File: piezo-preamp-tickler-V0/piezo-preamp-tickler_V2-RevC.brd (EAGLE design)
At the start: 160 x 100 mm, 41 parts, among them IC1 OPA2134UA, Q1 J201SOT-23, Q2 J201SOT-23, SW2-SPST INPUT-select

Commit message: piezo with buffer, mems with dual gain
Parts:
- removed D4: MMSZ5231B, CMU-ArtFab:SOD123
- removed D5: 1N4148, adafruit:SOD-123
- removed U$2: SWITCH_DPDT, CMU-ArtFab:SWITCH_DPDT_CL-SB-22B
- removed U$4: (no value), CMU-ArtFab:TRIMPOT-BOURNS-3306F
- added C5: 10uF, adafruit:C0805K
- added R18: 1M, adafruit:TC33X
- added SW1-DPDT: OUTPUT-select, microbuilder:DPDT_SMT_JS202011SCQN
- C1: value 150uF -> 10uF; device rcl:TT5D7L -> adafruit:C0805K
- C2: value 10uF -> 0.1uF
- C3: device adafruit:C0603 -> adafruit:C0805K
- C4: value 100uF -> 150uF; device rcl:TT5D7L -> adafruit:C050-024X044
- D1, D2: value MMSZ5231B -> (none); device CMU-ArtFab:SOD123 -> diode:SOD123
- D3: value MMSZ5231B -> 1N4148; device CMU-ArtFab:SOD123 -> adafruit:SOD-123
- R1: value 10M -> 2.2K
- R10: value 20K -> 1K; device adafruit:TC33X -> CMU-ArtFab:R0603
- R11: value 1K -> 10K
- R12: value 1M -> 390; device CMU-ArtFab:R0603 -> CMU-ArtFab:R0805
- R13: value 1.2K -> 10M
- R14: value 2.2K -> 1.2K
- R15: value 10 -> 1K
- R16: value 390 -> 10
- R3: value 10K -> 1M
- R9: value 1K -> 20K; device CMU-ArtFab:R0603 -> adafruit:TC33X
- moved D1 169.7 mm to (99.1, -1.27)
- moved D2 164.3 mm to (91.4, -1.27), turned to 0 degrees
- moved R1 153.8 mm to (90.2, 11.4), turned to 0 degrees
- moved R3 145.0 mm to (80.0, 6.35), turned to 0 degrees
- moved C1 141.6 mm to (74.9, -1.27), turned to 270 degrees
- moved R2 140.7 mm to (80.0, 11.4), turned to 0 degrees
- moved Q2 136.7 mm to (87.6, 6.35), turned to 180 degrees
- moved R7 131.4 mm to (74.9, 5.08), turned to 90 degrees
- moved R9 130.7 mm to (72.4, 10.2), turned to 180 degrees
- moved R17 128.8 mm to (80.0, -1.27)
- moved C6 123.3 mm to (54.6, 0.00), turned to 270 degrees
- moved Q1 122.6 mm to (50.8, 0.00)
- moved R10 115.3 mm to (80.0, 2.54)
- moved R11 110.8 mm to (59.7, 10.2)
- moved R12 100.5 mm to (34.3, -1.27), turned to 180 degrees
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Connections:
- net HEADSET-MIC renamed N$12
- removed net AMPILFIED-PIEZO: Q2.1, R14.2, SW2-SPST.P$3
- removed net N$1 (its old number): D3.A, D4.A
- new net SELECT: Q2.1, R1.2, SW2-SPST.P$3
- net +12V: now also D3.A; no longer D5.A
- net GND: now also C2.2, C4.2, C5.2, D2.C, R18.2, R3.1; no longer C1.-, C4.-, D1.C, D3.C, R12.1
- net N$10: now also D1.C, R10.1, R3.2; no longer D4.C, R11.1, R12.2
- net N$11: now also C1.2, R10.2, SW1-DPDT.P$3, SW1-DPDT.P$4; no longer C2.2, R11.2, U$2.3, U$2.6
- net N$13: now also SW1-DPDT.P$5; no longer U$2.5
- net N$14: now also C4.1, R14.2; no longer C1.+, R2.2
- net N$15: now also SW1-DPDT.P$2; no longer U$2.2
- net N$16: now also C5.1, D3.C, R16.2; no longer D5.C, R15.2
- net N$18: now also R12.1; no longer R16.1
- net N$2: now also R13.2, R18.3; no longer D2.C, R1.2
- net N$22: now also R15.1; no longer R8.1
- net N$23: now also R15.2; no longer R8.2
- net N$24: now also R8.1; no longer R9.1
- net N$25: now also C2.1, R11.2, R16.1; no longer C4.+, R15.1, R3.2
- net N$26: now also SW1-DPDT.P$1; no longer U$2.1
- net N$27: now also SW1-DPDT.P$6; no longer U$2.4
- net N$3: now also R2.2; no longer R13.2
- net N$6: now also C1.1, R9.2; no longer C2.1, R10.2
- net N$7: now also R8.2, R9.3; no longer R10.3, R9.2
- net N$9: now also R11.1; no longer R3.1
- net VBAT: now also R12.2; no longer R16.2
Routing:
- net GND: track 0.00 -> 159.7 mm, vias 0 -> 1
- net N$17: track 0.00 -> 90.8 mm, vias 0 -> 7
- net SELECT: track 0.00 -> 82.4 mm, vias 0 -> 3
- net N$25: track 0.00 -> 72.7 mm, vias 0 -> 3
- net VBAT: track 0.00 -> 67.1 mm, vias 0 -> 1
- net N$21: track 0.00 -> 56.0 mm
- net N$23: track 0.00 -> 53.4 mm, vias 0 -> 3
- net N$15: track 0.00 -> 48.6 mm, vias 0 -> 3
- net N$13: track 0.00 -> 45.1 mm, vias 0 -> 1
- net N$26: track 0.00 -> 44.4 mm, vias 0 -> 3
- net N$11: track 0.00 -> 38.1 mm, vias 0 -> 1
- net N$2: track 0.00 -> 38.0 mm, vias 0 -> 1
- net N$19: track 0.00 -> 37.9 mm
- net N$27: track 0.00 -> 33.2 mm, vias 0 -> 1
- net N$10: track 0.00 -> 29.3 mm, vias 0 -> 2
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- added copper zone on layer 1, net N$4
- added copper zone on layer 16, net N$8
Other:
- board size 160 x 100 mm -> 95 x 17.7 mm

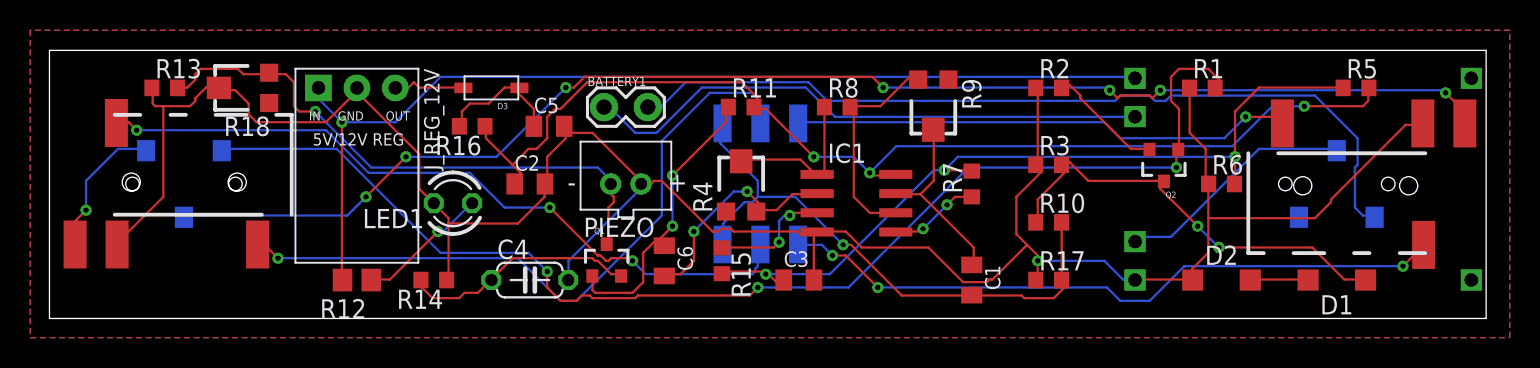
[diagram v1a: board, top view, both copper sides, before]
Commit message: piezo fix for version C
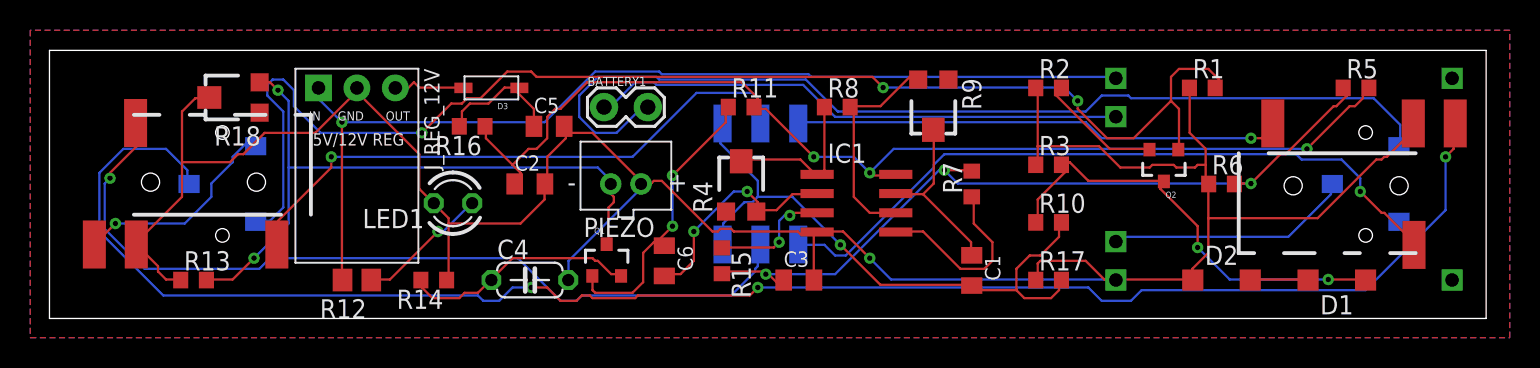
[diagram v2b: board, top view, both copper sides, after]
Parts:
- moved R13 12.8 mm to (23.5, -1.27)
- moved SW2-SPST 2.54 mm to (25.4, 5.08), turned to 270 degrees
- moved POWER 1.91 mm to (101.0, 5.08), turned to 270 degrees
- moved TO-HEADSET 1.27 mm to (19.1, 6.35)
- moved USB-LIPO-CHARGER 1.27 mm to (95.2, 5.08)
- moved R18 0.90 mm to (26.0, 10.8)
- moved C1 0.64 mm to (74.9, -0.64)
- moved TO-PHONE 0.63 mm to (104.8, 3.81)
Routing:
- net N$17: track 90.8 -> 112.9 mm, vias 7 -> 3
- net GND: track 159.7 -> 170.1 mm
- net N$21: track 56.0 -> 65.5 mm
- net N$15: track 48.6 -> 56.2 mm, vias 3 -> 1
- net N$5: track 5.98 -> 12.5 mm, vias 2 -> 0
- net N$13: track 45.1 -> 39.1 mm
- net N$2: track 38.0 -> 43.7 mm, vias 1 -> 2
- net N$12: track 9.41 -> 14.2 mm
- net SELECT: track 82.4 -> 87.0 mm
- net N$26: track 44.4 -> 47.2 mm, vias 3 -> 1
- net N$19: track 37.9 -> 35.5 mm
- net N$11: track 38.1 -> 40.2 mm
- net N$23: track 53.4 -> 52.3 mm
- net VBAT: track 67.1 -> 66.1 mm
- net N$10: track 29.3 -> 30.1 mm
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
